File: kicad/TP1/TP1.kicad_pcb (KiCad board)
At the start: 2 copper layers, 21 parts, among them P1 CONN_20X2, P2 CONN_20X2, U1 MPU-6050, U2 CR2013-MI2120, U4 LM386

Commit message: Actualizacion de KiCad
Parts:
- added ?: , , F.Cu at (64.4, 75.3)
- added ?: , , F.Cu at (65.2, 119.4)
- added ?: , , F.Cu at (103.4, 116.2)
- added ?: , , F.Cu at (81.3, 132.9)
- added ?: , , F.Cu at (81.3, 137.5)
- added ?: , , F.Cu at (77.5, 80.5)
- added ?: , , F.Cu at (80.0, 75.3)
- added ?: , , F.Cu at (68.7, 80.3)
- added ?: , , F.Cu at (99.1, 134.8)
- added ?: , , F.Cu at (99.1, 129.9)
- added ?: , , F.Cu at (106.4, 129.1)
- added ?: , , F.Cu at (106.5, 122.2)
- added ?: , , F.Cu at (99.2, 116.2)
- added ?: , , F.Cu at (77.7, 119.4)
- moved R2 18.2 mm to (85.0, 106.1), turned to -90 degrees
- moved C8 15.8 mm to (96.6, 99.1)
- moved R1 11.5 mm to (91.4, 67.9)
- moved C2 7.84 mm to (78.7, 122.0)
- moved C10 6.33 mm to (96.6, 106.7)
- moved U1 5.75 mm to (124.5, 127.0), turned to 180 degrees
- moved C3 1.33 mm to (99.1, 154.1)
- moved C1 1.21 mm to (78.7, 149.2)
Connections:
- P1 pad 1: unconnected-(P1-P1-Pad1) -> +3.3V
- P2 pad 1: +3.3V -> unconnected-(P2-P1-Pad1)
- P2 pad 29: GPIO_0 -> unconnected-(P2-P29-Pad29)
- P2 pad 31: GPIO_2 -> unconnected-(P2-P31-Pad31)
- P2 pad 33: GPIO_4 -> unconnected-(P2-P33-Pad33)
- P2 pad 35: GPIO_6 -> unconnected-(P2-P35-Pad35)
- P2 pad 36: unconnected-(P2-P36-Pad36) -> GPIO_5
- P2 pad 38: unconnected-(P2-P38-Pad38) -> GPIO_7
- P2 pad 40: unconnected-(P2-P40-Pad40) -> GPIO_8
- U2 pad 11: GPIO_0 -> GPIO_5
- U2 pad 12: GPIO_2 -> GPIO_7
- U2 pad 13: GPIO_4 -> GPIO_8
- U2 pad 2: GPIO_3 -> GPIO_1
- U2 pad 5: GPIO_1 -> GPIO_3
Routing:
- net GPIO_8: track 0.00 -> 109.3 mm
- net GPIO_7: track 0.00 -> 100.7 mm
- net GPIO_5: track 0.00 -> 91.7 mm
- net GPIO_4: track 81.8 -> 0.00 mm
- net GPIO_2: track 76.3 -> 0.00 mm
- net GPIO_0: track 70.3 -> 0.00 mm
- net GND: track 218.9 -> 244.6 mm, vias 0 -> 4
- net SPI_SCK: track 62.4 -> 88.0 mm, vias 0 -> 4
- net +3.3V: track 187.6 -> 162.2 mm
- net Net-(C2-Pad1): track 0.00 -> 20.9 mm
- net GPIO_3: track 52.1 -> 69.8 mm
- net DAC: track 73.8 -> 89.4 mm
- net Net-(U2-LED): track 24.3 -> 39.6 mm
- net +5V: track 86.8 -> 99.3 mm
- net I2C_SDA: track 18.9 -> 6.75 mm
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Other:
- board outline added: 86.4 x 137.2 mm

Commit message: Actualizacion Kicad
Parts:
- C1: footprint Capacitor_THT:C_Disc_D5.0mm_W2.5mm_P5.00mm -> Capacitor_THT:CP_Radial_D8.0mm_P5.00mm
- RV1: footprint Potentiometer_THT:Potentiometer_Piher_PT-6-V_Vertical -> Potentiometer_THT:Potentiometer_Bourns_3296W_Vertical
- moved R1 7.62 mm to (83.8, 67.9)
- moved RV1 6.95 mm to (91.4, 160.0), turned to 0 degrees
- moved C6 6.90 mm to (85.1, 147.2)
- moved C7 6.90 mm to (92.1, 147.2)
- moved ? 0.31 mm to (81.3, 137.2)
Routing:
- net Net-(U2-LED): track 39.6 -> 32.1 mm
- net +5V: track 99.3 -> 92.4 mm
- net Net-(U4-BYPASS): track 15.1 -> 8.18 mm
- net DAC: track 89.4 -> 85.2 mm
- net Net-(C3-Pad1): track 18.1 -> 15.6 mm
- net GND: track 244.6 -> 243.2 mm
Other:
- board text added: "A"
- board text added: "C"
- board text added: "D"
- board text added: "E"
- board text added: "G"
- board text added: "M"
- board text added: "P E R E I R A"
- board text added: "Í"
- board text removed: "GIT MR PU"

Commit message: patch 2
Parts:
- added ?: , , F.Cu at (64.7, 93.2)
- added ?: , , F.Cu at (64.8, 88.1)
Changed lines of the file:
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@@
 		(tags "Potentiometer vertical Bourns 3296W")
 		(property "Reference" "RV1"
-			(at -2.54 -3.66 360)
+			(at -2.54 -3.66 0)
 			(layer "F.SilkS")
 			(effects
@@
 		)
 		(property "Value" "10k"
-			(at -2.54 3.67 360)
+			(at -2.54 3.67 0)
 			(layer "F.Fab")
 			(effects
@@
 		)
 		(fp_text user "${REFERENCE}"
-			(at -3.175 0.005 360)
+			(at -3.175 0.005 0)
 			(layer "F.Fab")
 			(effects
@@
 		(pad "1" thru_hole circle
 			(at 0 0)
-			(size 1.44 1.44)
-			(drill 0.8)
+			(size 2 2)
+			(drill 0.7)
 			(layers "*.Cu" "*.Mask")
 			(remove_unused_layers no)
@@
 		(pad "2" thru_hole circle
 			(at -2.54 0)
-			(size 1.44 1.44)
-			(drill 0.8)
+			(size 2 2)
+			(drill 0.7)
 			(layers "*.Cu" "*.Mask")
 			(remove_unused_layers no)
@@
 		(pad "3" thru_hole circle
 			(at -5.08 0)
-			(size 1.44 1.44)
-			(drill 0.8)
+			(size 2 2)
+			(drill 0.7)
 			(layers "*.Cu" "*.Mask")
 			(remove_unused_layers no)
@@
 		)
 	)
+	(footprint ""
+		(layer "F.Cu")
+		(at 64.734784 93.184869)
+		(property "Reference" ""
+			(at 0 0 0)
+			(layer "F.SilkS")
+			(effects
+				(font
+					(size 1.27 1.27)
+					(thickness 0.15)
+				)
+			)
+		)
+		(property "Value" ""
+			(at 0 0 0)
+			(layer "F.Fab")
+			(effects
+				(font
+					(size 1.27 1.27)
+					(thickness 0.15)
+				)
+			)
+		)
+		(property "Footprint" ""
+			(at 0 0 0)
+			(layer "F.Fab")
+			(hide yes)
+			(effects
+				(font
+					(size 1.27 1.27)
+					(thickness 0.15)
+				)
+			)
+		)
+		(property "Datasheet" ""
+			(at 0 0 0)
+			(layer "F.Fab")
+			(hide yes)
+			(effects
+				(font
+					(size 1.27 1.27)
+					(thickness 0.15)
+				)
+			)
+		)
+		(property "Description" ""
+			(at 0 0 0)
+			(layer "F.Fab")
+			(hide yes)
+			(effects
+				(font
+					(size 1.27 1.27)
+					(thickness 0.15)
+				)
+			)
+		)
+		(pad "" thru_hole circle
+			(at 0 0 90)
+			(size 2 2)
+			(drill 0.7)
+			(layers "*.Cu" "*.Mask")
+			(remove_unused_layers no)
+			(pintype "passive")
+		)
+	)
 	(footprint "Capacitor_THT:CP_Radial_D8.0mm_P5.00mm"
 		(layer "F.Cu")
@@
 		(pad "1" thru_hole rect
 			(at 0 0 270)
-			(size 1.6 1.6)
-			(drill 0.8)
+			(size 2 2)
+			(drill 0.7)
 			(layers "*.Cu" "*.Mask")
 			(remove_unused_layers no)
@@
 		(pad "2" thru_hole circle
 			(at 5 0 270)
-			(size 1.6 1.6)
-			(drill 0.8)
+			(size 2 2)
+			(drill 0.7)
 			(layers "*.Cu" "*.Mask")
 			(remove_unused_layers no)
@@
 		)
 	)
+	(footprint ""
+		(layer "F.Cu")
+		(at 64.78316 88.056966)
+		(property "Reference" ""
+			(at 0 0 0)
+			(layer "F.SilkS")
+			(effects
+				(font
+					(size 1.27 1.27)
+					(thickness 0.15)
+				)
+			)
+		)
+		(property "Value" ""
+			(at 0 0 0)
+			(layer "F.Fab")
+			(effects
+				(font
+					(size 1.27 1.27)
+					(thickness 0.15)
+				)
+			)
+		)
+		(property "Footprint" ""
+			(at 0 0 0)
+			(layer "F.Fab")
+			(hide yes)
+			(effects
+				(font
+					(size 1.27 1.27)
+					(thickness 0.15)
+				)
+			)
+		)
+		(property "Datasheet" ""
+			(at 0 0 0)
+			(layer "F.Fab")
+			(hide yes)
+			(effects
+				(font
+					(size 1.27 1.27)
+					(thickness 0.15)
+				)
+			)
+		)
+		(property "Description" ""
+			(at 0 0 0)
+			(layer "F.Fab")
+			(hide yes)
+			(effects
+				(font
+					(size 1.27 1.27)
+					(thickness 0.15)
+				)
+			)
+		)
+		(pad "" thru_hole circle
+			(at 0 0 90)
+			(size 2 2)
+			(drill 0.7)
+			(layers "*.Cu" "*.Mask")
+			(remove_unused_layers no)
+			(pintype "passive")
+		)
+	)
 	(footprint "Capacitor_THT:C_Disc_D5.0mm_W2.5mm_P5.00mm"
 		(layer "F.Cu")
@@
 		(layer "B.Cu")
 	)
+	(gr_line
+		(start 105.85419 69.814441)
+		(end 102.854851 69.814441)
+		(stroke
+			(width 0.5)
+			(type default)
+		)
+		(layer "B.Cu")
+	)
 	(gr_circle
 		(center 110.502882 46.99)
@@
 		(end 102.854851 69.814441)
 		(stroke
-			(width 0.5)
-			(type default)
-		)
-		(layer "B.Cu")
-	)
-	(gr_line
-		(start 105.85419 69.814441)
-		(end 102.854851 69.814441)
-		(stroke

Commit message: KiCad
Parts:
- added ?: , , F.Cu at (58.1, 165.1)
- added ?: , , F.Cu at (134.5, 165.1)
- added ?: , , F.Cu at (58.1, 37.8)
- added ?: , , F.Cu at (134.4, 37.6)
- added G***: LOGO, Puncho_Esqueleto:Logo_Poncho, F.Cu at (121.9, 154.9)
- moved G101 17.5 mm to (121.9, 164.2)

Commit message: a
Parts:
- removed G***: LOGO, Puncho_Esqueleto:Logo_Poncho
- moved G101 2.63 mm to (122.0, 161.5)

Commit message: Sacar acentto
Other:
- board text added: "I"
- board text removed: "Í"
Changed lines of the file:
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@@
 		)
 	)
-	(gr_text "Í"
+	(gr_text "I"
 		(at 102.647214 81.283317 0)
 		(layer "B.Cu")

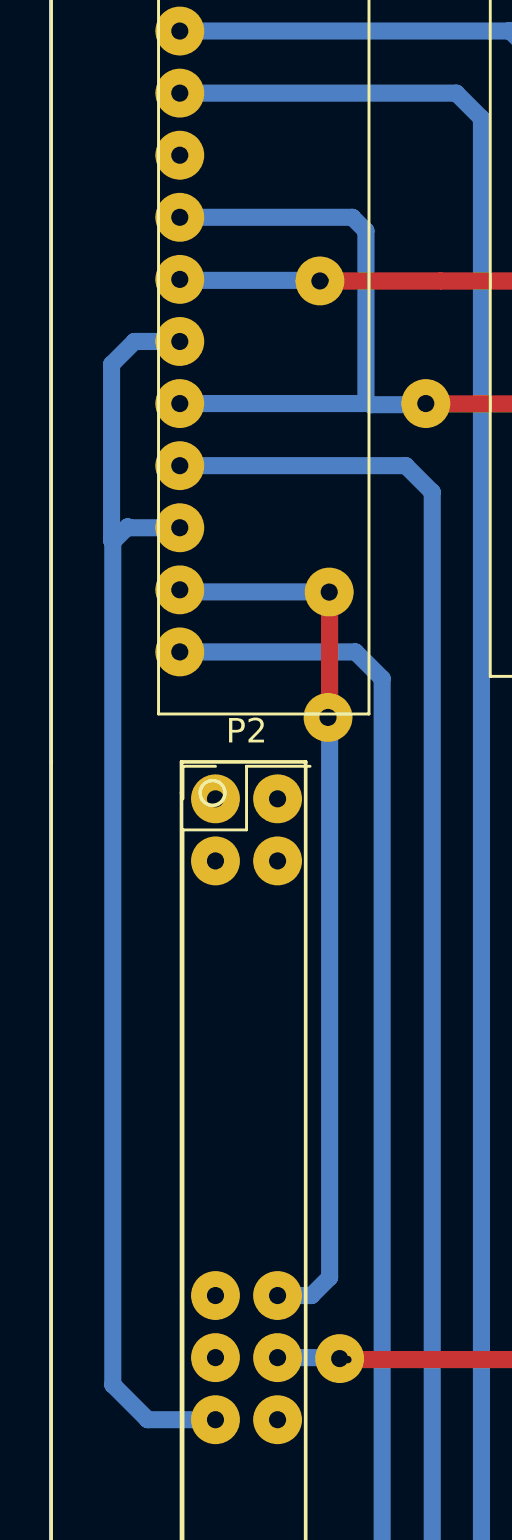
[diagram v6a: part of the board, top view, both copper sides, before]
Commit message: Correcciones del CAD
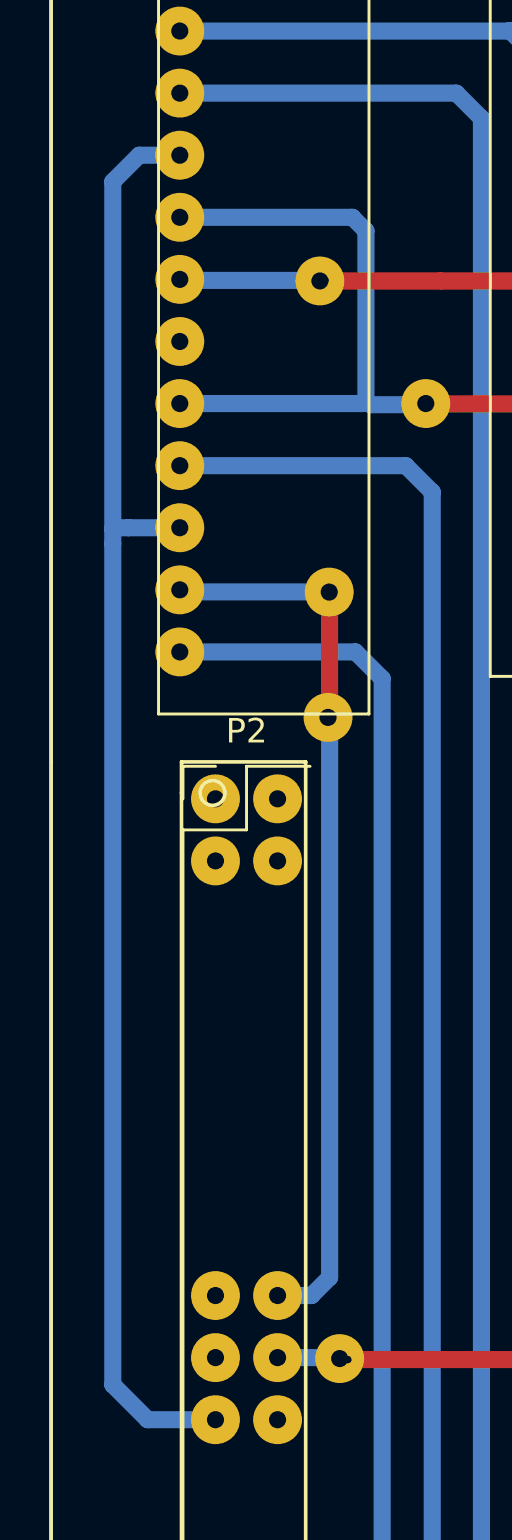
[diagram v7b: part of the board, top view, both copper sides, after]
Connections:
- U2 pad 10: unconnected-(U2-SDI(MOSI)-Pad10) -> SPI_MOSI
- U2 pad 7: SPI_MOSI -> unconnected-(U2-SDO(MISO)-Pad7)
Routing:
- net SPI_MOSI: track 52.7 -> 60.0 mm
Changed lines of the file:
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@@
 	(net 44 "unconnected-(U2-SD_MOSI-Pad15)")
 	(net 45 "unconnected-(U2-SD_SCK-Pad17)")
-	(net 46 "unconnected-(U2-SDI(MOSI)-Pad10)")
+	(net 46 "unconnected-(U2-SDO(MISO)-Pad7)")
 	(net 47 "unconnected-(U2-SD_MISO-Pad16)")
 	(net 48 "unconnected-(U2-SD_CS-Pad14)")
@@
 			(layers "*.Cu" "*.Mask")
 			(remove_unused_layers no)
-			(net 27 "SPI_MOSI")
+			(net 46 "unconnected-(U2-SDO(MISO)-Pad7)")
 			(pinfunction "SDO(MISO)")
-			(pintype "output")
+			(pintype "output+no_connect")
 		)
 		(pad "8" thru_hole circle
@@
 			(layers "*.Cu" "*.Mask")
 			(remove_unused_layers no)
-			(net 46 "unconnected-(U2-SDI(MOSI)-Pad10)")
+			(net 27 "SPI_MOSI")
 			(pinfunction "SDI(MOSI)")
-			(pintype "bidirectional+no_connect")
+			(pintype "bidirectional")
 		)
 		(pad "11" thru_hole circle
@@
 	)
 	(segment
-		(start 55.929175 120.486343)
-		(end 55.929175 85.996865)
+		(start 55.929175 86.073557)
+		(end 55.929175 85.467498)
 		(width 0.7)
 		(layer "B.Cu")
@@
 	)
 	(segment
-		(start 60.130452 121.915073)
-		(end 57.357905 121.915073)
+		(start 55.9716 85.425073)
+		(end 55.929175 85.467498)
 		(width 0.7)
 		(layer "B.Cu")
@@
 	)
 	(segment
-		(start 55.929175 85.996865)
-		(end 56.539313 85.386727)
+		(start 57.357905 121.915073)
+		(end 55.929175 120.486343)
 		(width 0.7)
 		(layer "B.Cu")
@@
 	(segment
 		(start 56.577659 85.425073)
-		(end 58.670452 85.425073)
+		(end 55.9716 85.425073)
 		(width 0.7)
 		(layer "B.Cu")
@@
 	)
 	(segment
-		(start 56.539313 85.386727)
-		(end 56.577659 85.425073)
+		(start 55.929175 71.26671)
+		(end 57.010812 70.185073)
 		(width 0.7)
 		(layer "B.Cu")
@@
 	)
 	(segment
-		(start 55.88 85.94769)
-		(end 55.929175 85.996865)
+		(start 56.577659 85.425073)
+		(end 58.670452 85.425073)
 		(width 0.7)
 		(layer "B.Cu")
@@
 	)
 	(segment
-		(start 57.357905 121.915073)
-		(end 55.929175 120.486343)
+		(start 57.010812 70.185073)
+		(end 58.670452 70.185073)
 		(width 0.7)
 		(layer "B.Cu")
@@
 	)
 	(segment
-		(start 55.88 78.74)
-		(end 55.88 85.94769)
+		(start 60.130452 121.915073)
+		(end 57.357905 121.915073)
 		(width 0.7)
 		(layer "B.Cu")
@@
 	)
 	(segment
-		(start 58.670452 77.805073)
-		(end 56.814927 77.805073)
+		(start 55.929175 120.486343)
+		(end 55.929175 86.073557)
 		(width 0.7)
 		(layer "B.Cu")
@@
 	)
 	(segment
-		(start 56.814927 77.805073)
-		(end 55.88 78.74)
+		(start 55.929175 85.467498)
+		(end 55.929175 71.26671)
 		(width 0.7)
 		(layer "B.Cu")
